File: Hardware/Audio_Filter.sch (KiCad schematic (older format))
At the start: 26 parts, among them U12 NE5534, U13 NE5534, U14 NE5534

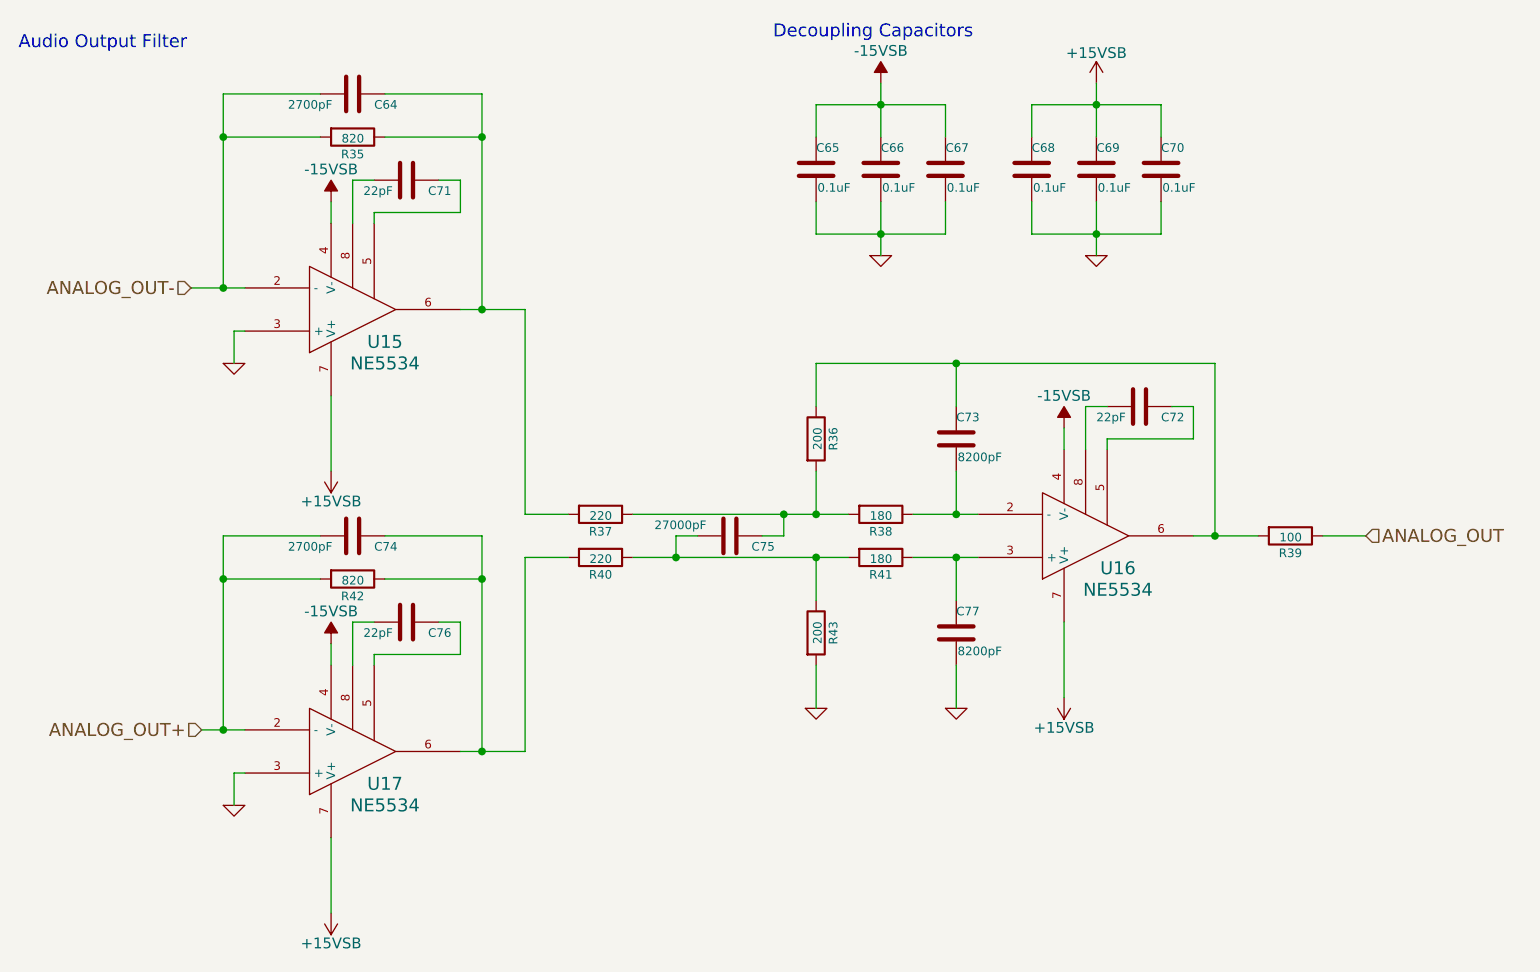
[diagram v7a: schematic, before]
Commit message: Updated libraries and place components into board layout
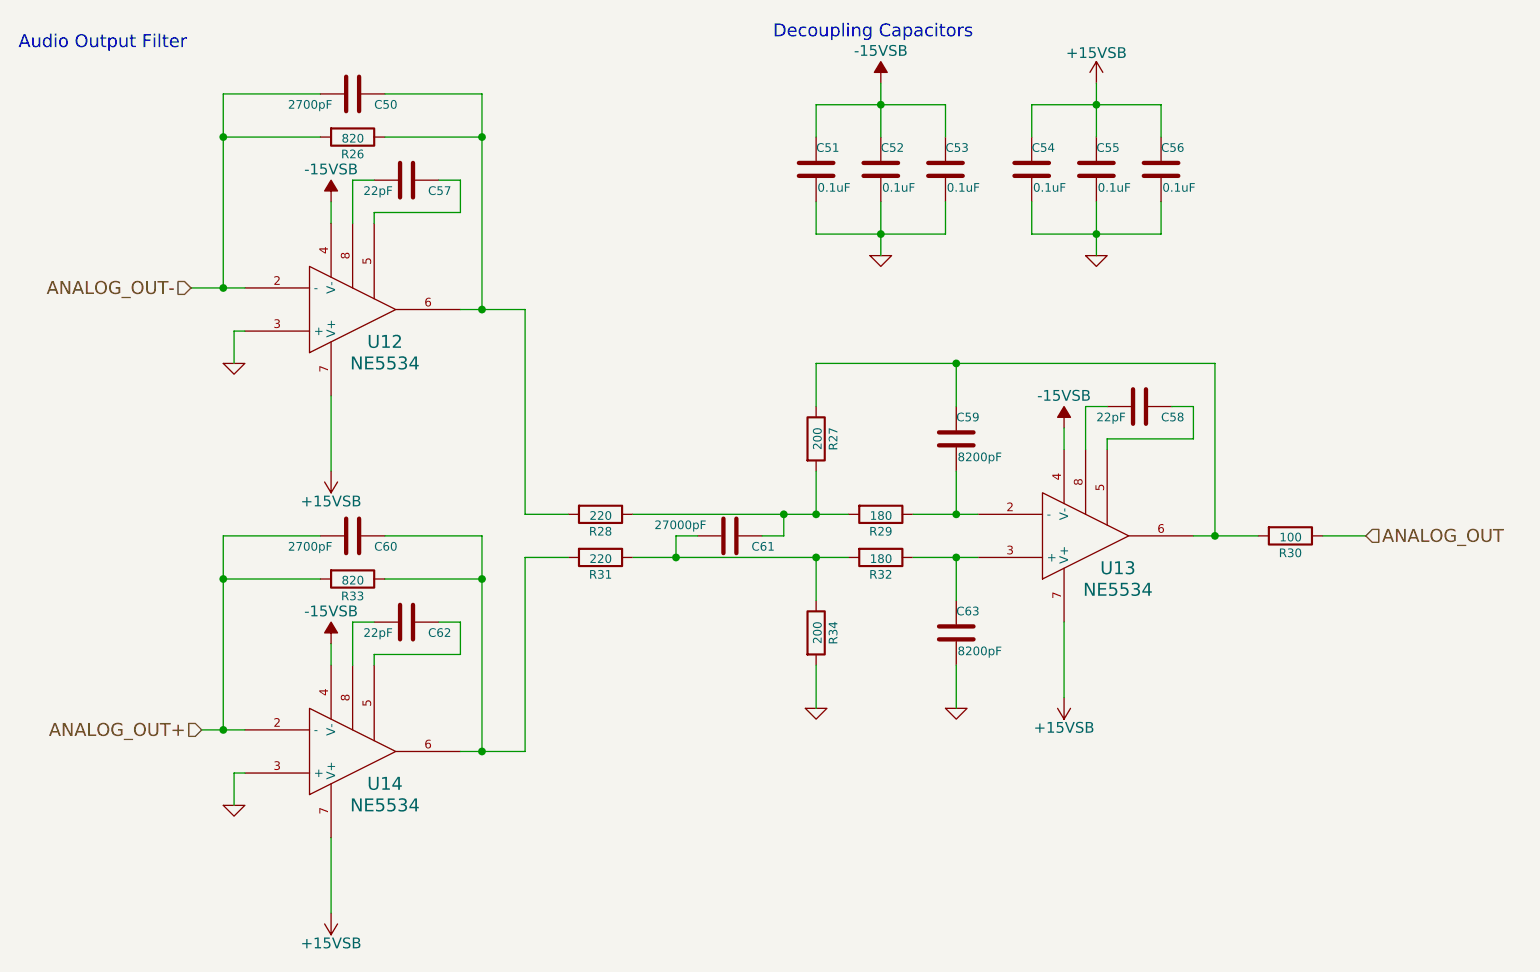
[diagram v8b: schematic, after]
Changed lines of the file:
@@
 AR Path="/57F89F43/57F8A539/57B0E0AF" Ref="C50"  Part="1"
 AR Path="/57F89F43/57F8A547/57B0E0AF" Ref="C64"  Part="1"
-F 0 "C64" V 3750 2300 40  0000 L CNN
+F 0 "C50" V 3750 2300 40  0000 L CNN
 F 1 "2700pF" V 3750 1900 40  0000 L CNN
 F 2 "Capacitors_SMD:C_0402" H 3738 2050 30  0001 C CNN
@@
 AR Path="/57F89F43/57F8A539/57B0E0B6" Ref="R26"  Part="1"
 AR Path="/57F89F43/57F8A547/57B0E0B6" Ref="R35"  Part="1"
-F 0 "R35" V 3780 2400 40  0000 C CNN
+F 0 "R26" V 3780 2400 40  0000 C CNN
 F 1 "820" V 3707 2401 40  0000 C CNN
 F 2 "Resistors_SMD:R_0402" V 3630 2400 30  0001 C CNN
@@
 AR Path="/57F89F43/57F8A539/57B0E0C8" Ref="C57"  Part="1"
 AR Path="/57F89F43/57F8A547/57B0E0C8" Ref="C71"  Part="1"
-F 0 "C71" V 4000 2700 40  0000 L CNN
+F 0 "C57" V 4000 2700 40  0000 L CNN
 F 1 "22pF" V 4000 2400 40  0000 L CNN
 F 2 "Capacitors_SMD:C_0402" H 3988 2450 30  0001 C CNN
@@
 AR Path="/57F89F43/57F8A539/57B0E0E8" Ref="C60"  Part="1"
 AR Path="/57F89F43/57F8A547/57B0E0E8" Ref="C74"  Part="1"
-F 0 "C74" V 3750 4350 40  0000 L CNN
+F 0 "C60" V 3750 4350 40  0000 L CNN
 F 1 "2700pF" V 3750 3950 40  0000 L CNN
 F 2 "Capacitors_SMD:C_0603" H 3738 4100 30  0001 C CNN
@@
 AR Path="/57F89F43/57F8A539/57B0E0EF" Ref="R33"  Part="1"
 AR Path="/57F89F43/57F8A547/57B0E0EF" Ref="R42"  Part="1"
-F 0 "R42" V 3780 4450 40  0000 C CNN
+F 0 "R33" V 3780 4450 40  0000 C CNN
 F 1 "820" V 3707 4451 40  0000 C CNN
 F 2 "Resistors_SMD:R_0402" V 3630 4450 30  0001 C CNN
@@
 AR Path="/57F89F43/57F8A539/57B0E101" Ref="R31"  Part="1"
 AR Path="/57F89F43/57F8A547/57B0E101" Ref="R40"  Part="1"
-F 0 "R40" V 4930 4350 40  0000 C CNN
+F 0 "R31" V 4930 4350 40  0000 C CNN
 F 1 "220" V 4857 4351 40  0000 C CNN
 F 2 "Resistors_SMD:R_0402" V 4780 4350 30  0001 C CNN
@@
 AR Path="/57F89F43/57F8A539/57B0E108" Ref="R28"  Part="1"
 AR Path="/57F89F43/57F8A547/57B0E108" Ref="R37"  Part="1"
-F 0 "R37" V 4930 4150 40  0000 C CNN
+F 0 "R28" V 4930 4150 40  0000 C CNN
 F 1 "220" V 4857 4151 40  0000 C CNN
 F 2 "Resistors_SMD:R_0402" V 4780 4150 30  0001 C CNN
@@
 AR Path="/57F89F43/57F8A539/57B0E115" Ref="C61"  Part="1"
 AR Path="/57F89F43/57F8A547/57B0E115" Ref="C75"  Part="1"
-F 0 "C75" V 5500 4350 40  0000 L CNN
+F 0 "C61" V 5500 4350 40  0000 L CNN
 F 1 "27000pF" V 5400 3900 40  0000 L CNN
 F 2 "Capacitors_SMD:C_0402" H 5488 4100 30  0001 C CNN
@@
 AR Path="/57F89F43/57F8A539/57B0E122" Ref="R29"  Part="1"
 AR Path="/57F89F43/57F8A547/57B0E122" Ref="R38"  Part="1"
-F 0 "R38" V 6230 4150 40  0000 C CNN
+F 0 "R29" V 6230 4150 40  0000 C CNN
 F 1 "180" V 6157 4151 40  0000 C CNN
 F 2 "Resistors_SMD:R_0402" V 6080 4150 30  0001 C CNN
@@
 AR Path="/57F89F43/57F8A539/57B0E129" Ref="R32"  Part="1"
 AR Path="/57F89F43/57F8A547/57B0E129" Ref="R41"  Part="1"
-F 0 "R41" V 6230 4350 40  0000 C CNN
+F 0 "R32" V 6230 4350 40  0000 C CNN
 F 1 "180" V 6157 4351 40  0000 C CNN
 F 2 "Resistors_SMD:R_0402" V 6080 4350 30  0001 C CNN
@@
 AR Path="/57F89F43/57F8A539/57B0E13A" Ref="R34"  Part="1"
 AR Path="/57F89F43/57F8A547/57B0E13A" Ref="R43"  Part="1"
-F 0 "R43" V 5930 4700 40  0000 C CNN
+F 0 "R34" V 5930 4700 40  0000 C CNN
 F 1 "200" V 5857 4701 40  0000 C CNN
 F 2 "Resistors_SMD:R_0402" V 5780 4700 30  0001 C CNN
@@
 AR Path="/57F89F43/57F8A539/57B0E143" Ref="R27"  Part="1"
 AR Path="/57F89F43/57F8A547/57B0E143" Ref="R36"  Part="1"
-F 0 "R36" V 5930 3800 40  0000 C CNN
+F 0 "R27" V 5930 3800 40  0000 C CNN
 F 1 "200" V 5857 3801 40  0000 C CNN
 F 2 "Resistors_SMD:R_0402" V 5780 3800 30  0001 C CNN
@@
 AR Path="/57F89F43/57F8A539/57B0E14C" Ref="C59"  Part="1"
 AR Path="/57F89F43/57F8A547/57B0E14C" Ref="C73"  Part="1"
-F 0 "C73" H 6500 3900 40  0000 L CNN
+F 0 "C59" H 6500 3900 40  0000 L CNN
 F 1 "8200pF" H 6506 3715 40  0000 L CNN
 F 2 "Capacitors_SMD:C_0402" H 6538 3650 30  0001 C CNN
@@
 AR Path="/57F89F43/57F8A539/57B0E155" Ref="C63"  Part="1"
 AR Path="/57F89F43/57F8A547/57B0E155" Ref="C77"  Part="1"
-F 0 "C77" H 6500 4800 40  0000 L CNN
+F 0 "C63" H 6500 4800 40  0000 L CNN
 F 1 "8200pF" H 6506 4615 40  0000 L CNN
 F 2 "Capacitors_SMD:C_0402" H 6538 4550 30  0001 C CNN
@@
 AR Path="/57F89F43/57F8A539/57B0E165" Ref="U12"  Part="1"
 AR Path="/57F89F43/57F8A547/57B0E165" Ref="U15"  Part="1"
-F 0 "U15" H 3850 3350 60  0000 C CNN
+F 0 "U12" H 3850 3350 60  0000 C CNN
 F 1 "NE5534" H 3850 3450 60  0000 C CNN
 F 2 "Housings_SOIC:SOIC-8_3.9x4.9mm_Pitch1.27mm" H 3700 3200 60  0001 C CNN
@@
 AR Path="/57F89F43/57F8A539/57B0E172" Ref="C62"  Part="1"
 AR Path="/57F89F43/57F8A547/57B0E172" Ref="C76"  Part="1"
-F 0 "C76" V 4000 4750 40  0000 L CNN
+F 0 "C62" V 4000 4750 40  0000 L CNN
 F 1 "22pF" V 4000 4450 40  0000 L CNN
 F 2 "Capacitors_SMD:C_0402" H 3988 4500 30  0001 C CNN
@@
 AR Path="/57F89F43/57F8A539/57B0E179" Ref="U14"  Part="1"
 AR Path="/57F89F43/57F8A547/57B0E179" Ref="U17"  Part="1"
-F 0 "U17" H 3850 5400 60  0000 C CNN
+F 0 "U14" H 3850 5400 60  0000 C CNN
 F 1 "NE5534" H 3850 5500 60  0000 C CNN
 F 2 "Housings_SOIC:SOIC-8_3.9x4.9mm_Pitch1.27mm" H 3700 5250 60  0001 C CNN
@@
 AR Path="/57F89F43/57F8A539/57B0E186" Ref="U13"  Part="1"
 AR Path="/57F89F43/57F8A547/57B0E186" Ref="U16"  Part="1"
-F 0 "U16" H 7250 4400 60  0000 C CNN
+F 0 "U13" H 7250 4400 60  0000 C CNN
 F 1 "NE5534" H 7250 4500 60  0000 C CNN
 F 2 "Housings_SOIC:SOIC-8_3.9x4.9mm_Pitch1.27mm" H 7100 4250 60  0001 C CNN
@@
 AR Path="/57F89F43/57F8A539/57B0E19A" Ref="C58"  Part="1"
 AR Path="/57F89F43/57F8A547/57B0E19A" Ref="C72"  Part="1"
-F 0 "C72" V 7400 3750 40  0000 L CNN
+F 0 "C58" V 7400 3750 40  0000 L CNN
 F 1 "22pF" V 7400 3450 40  0000 L CNN
 F 2 "Capacitors_SMD:C_0402" H 7388 3500 30  0001 C CNN
@@
 AR Path="/57F89F43/57F8A539/57B0E1AD" Ref="R30"  Part="1"
 AR Path="/57F89F43/57F8A547/57B0E1AD" Ref="R39"  Part="1"
-F 0 "R39" V 8130 4250 40  0000 C CNN
+F 0 "R30" V 8130 4250 40  0000 C CNN
 F 1 "100" V 8057 4251 40  0000 C CNN
 F 2 "Resistors_SMD:R_0402" V 7980 4250 30  0001 C CNN
@@
 AR Path="/57F89F43/57F8A539/57DC1736" Ref="#PWR80"  Part="1"
 AR Path="/57F89F43/57F8A547/57DC1736" Ref="#PWR94"  Part="1"
-F 0 "#PWR94" H 3600 2800 50  0001 C CNN
+F 0 "#PWR80" H 3600 2800 50  0001 C CNN
 F 1 "-15VSB" H 3600 2850 50  0000 C CNN
 F 2 "" H 3600 2700 50  0000 C CNN
@@
 AR Path="/57F89F43/57F8A539/57DC189C" Ref="#PWR86"  Part="1"
 AR Path="/57F89F43/57F8A547/57DC189C" Ref="#PWR100"  Part="1"
-F 0 "#PWR100" H 3600 4850 50  0001 C CNN
+F 0 "#PWR86" H 3600 4850 50  0001 C CNN
 F 1 "-15VSB" H 3600 4900 50  0000 C CNN
 F 2 "" H 3600 4750 50  0000 C CNN
@@
 AR Path="/57F89F43/57F8A539/57DC1A61" Ref="#PWR84"  Part="1"
 AR Path="/57F89F43/57F8A547/57DC1A61" Ref="#PWR98"  Part="1"
-F 0 "#PWR98" H 7000 3850 50  0001 C CNN
+F 0 "#PWR84" H 7000 3850 50  0001 C CNN
 F 1 "-15VSB" H 7000 3900 50  0000 C CNN
 F 2 "" H 7000 3750 50  0000 C CNN
@@
 AR Path="/57F89F43/57F8A539/57F9FAAF" Ref="C51"  Part="1"
 AR Path="/57F89F43/57F8A547/57F9FAAF" Ref="C65"  Part="1"
-F 0 "C65" H 5850 2650 40  0000 L CNN
+F 0 "C51" H 5850 2650 40  0000 L CNN
 F 1 "0.1uF" H 5856 2465 40  0000 L CNN
 F 2 "Capacitors_SMD:C_0402" H 5888 2400 30  0001 C CNN
@@
 AR Path="/57F89F43/57F8A539/57F9FABD" Ref="C52"  Part="1"
 AR Path="/57F89F43/57F8A547/57F9FABD" Ref="C66"  Part="1"
-F 0 "C66" H 6150 2650 40  0000 L CNN
+F 0 "C52" H 6150 2650 40  0000 L CNN
 F 1 "0.1uF" H 6156 2465 40  0000 L CNN
 F 2 "Capacitors_SMD:C_0402" H 6188 2400 30  0001 C CNN
@@
 AR Path="/57F89F43/57F8A539/57F9FAD1" Ref="C53"  Part="1"
 AR Path="/57F89F43/57F8A547/57F9FAD1" Ref="C67"  Part="1"
-F 0 "C67" H 6450 2650 40  0000 L CNN
+F 0 "C53" H 6450 2650 40  0000 L CNN
 F 1 "0.1uF" H 6456 2465 40  0000 L CNN
 F 2 "Capacitors_SMD:C_0402" H 6488 2400 30  0001 C CNN
@@
 AR Path="/57F89F43/57F8A539/57FA1599" Ref="C54"  Part="1"
 AR Path="/57F89F43/57F8A547/57FA1599" Ref="C68"  Part="1"
-F 0 "C68" H 6850 2650 40  0000 L CNN
+F 0 "C54" H 6850 2650 40  0000 L CNN
 F 1 "0.1uF" H 6856 2465 40  0000 L CNN
 F 2 "Capacitors_SMD:C_0402" H 6888 2400 30  0001 C CNN
@@
 AR Path="/57F89F43/57F8A539/57FA15A7" Ref="C55"  Part="1"
 AR Path="/57F89F43/57F8A547/57FA15A7" Ref="C69"  Part="1"
-F 0 "C69" H 7150 2650 40  0000 L CNN
+F 0 "C55" H 7150 2650 40  0000 L CNN
 F 1 "0.1uF" H 7156 2465 40  0000 L CNN
 F 2 "Capacitors_SMD:C_0402" H 7188 2400 30  0001 C CNN
@@
 AR Path="/57F89F43/57F8A539/57FA15BB" Ref="C56"  Part="1"
 AR Path="/57F89F43/57F8A547/57FA15BB" Ref="C70"  Part="1"
-F 0 "C70" H 7450 2650 40  0000 L CNN
+F 0 "C56" H 7450 2650 40  0000 L CNN
 F 1 "0.1uF" H 7456 2465 40  0000 L CNN
 F 2 "Capacitors_SMD:C_0402" H 7488 2400 30  0001 C CNN
@@
 AR Path="/57F89F43/57F8A539/57FFFBE8" Ref="#PWR78"  Part="1"
 AR Path="/57F89F43/57F8A547/57FFFBE8" Ref="#PWR92"  Part="1"
-F 0 "#PWR92" H 6150 2250 50  0001 C CNN
+F 0 "#PWR78" H 6150 2250 50  0001 C CNN
 F 1 "-15VSB" H 6150 2300 50  0000 C CNN
 F 2 "" H 6150 2150 50  0000 C CNN
